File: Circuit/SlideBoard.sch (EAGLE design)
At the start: 24 parts

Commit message: Updated controller board to include BLE112 for easier soldering
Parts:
- R3: value 10k -> 50k
- U$1: value BLE113 -> BLE112; device Random:BLE113 -> temp:BLE112
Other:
- moved on the sheet: CAM, FOCUS, LIM, R3, R5, R6, RESET, SHUTTER, UART

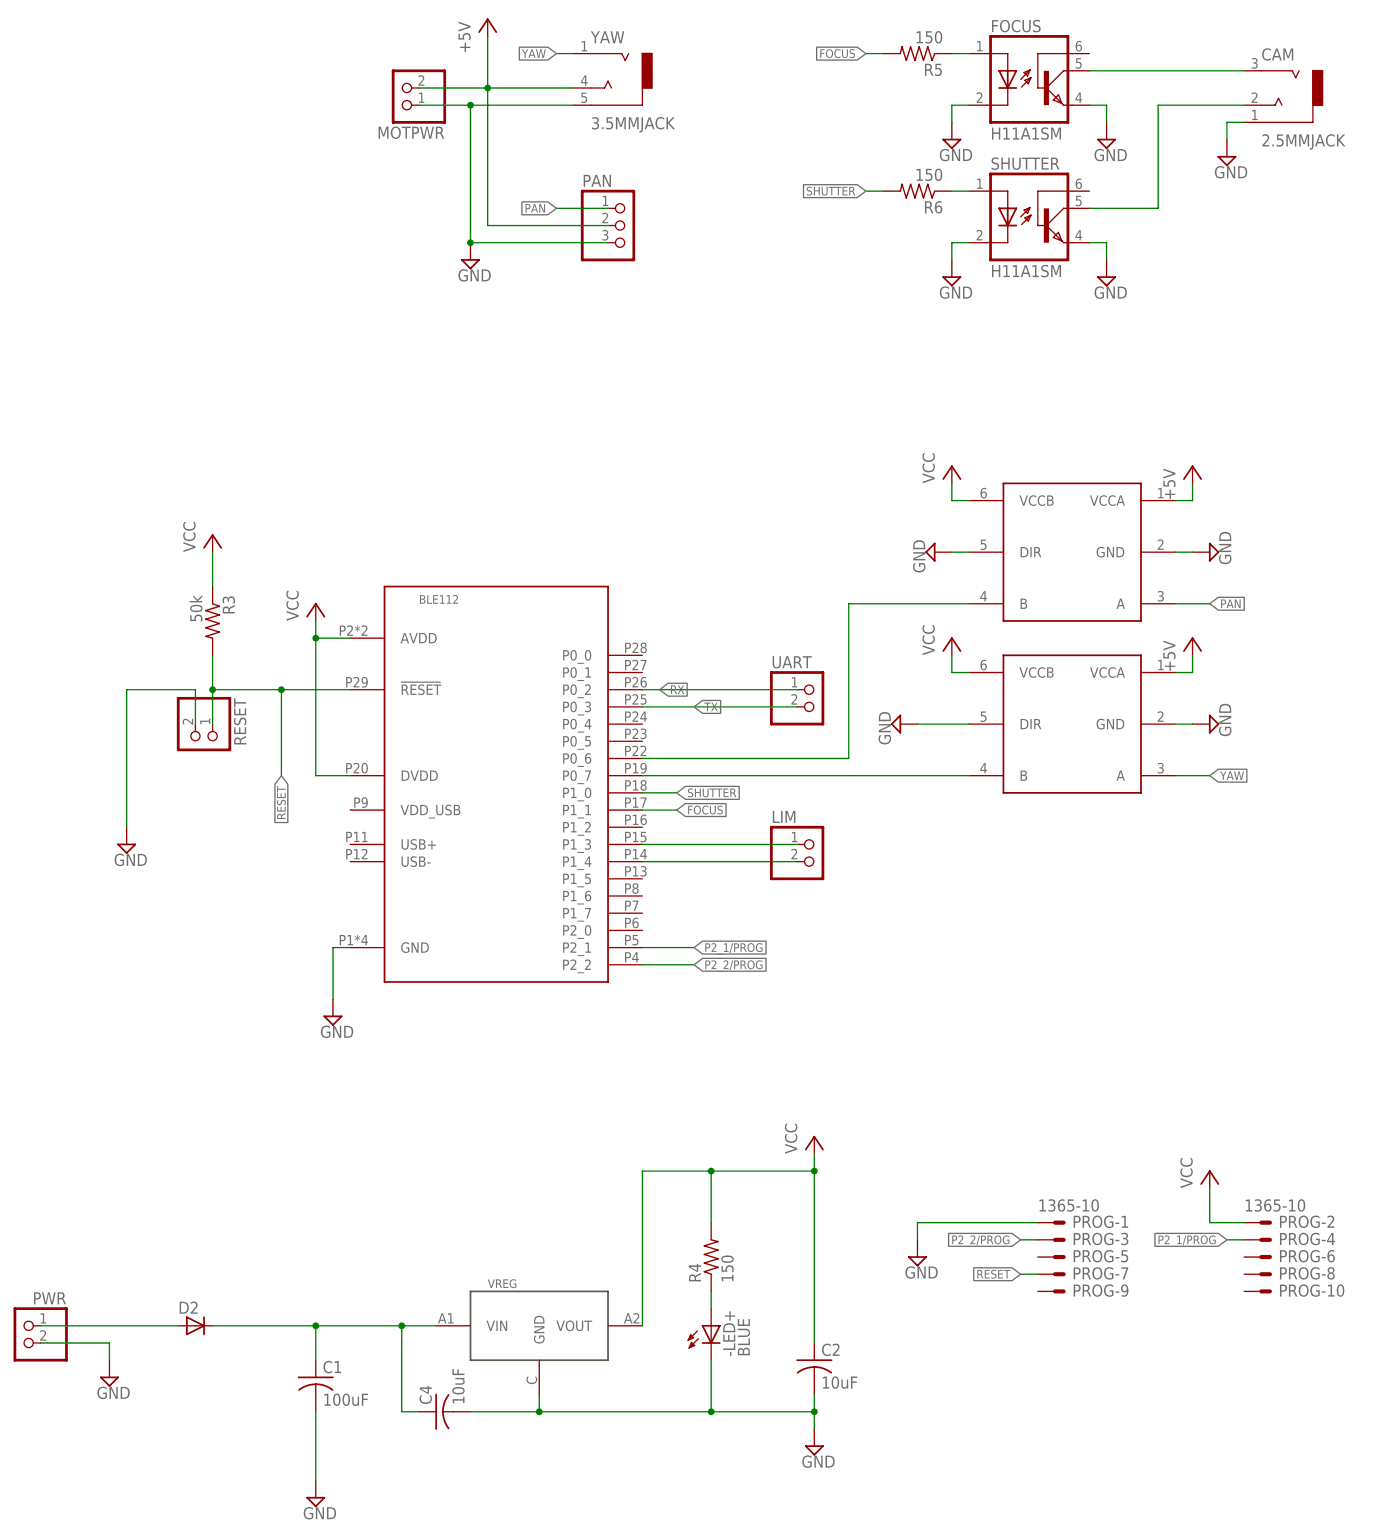
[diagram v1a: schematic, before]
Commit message: Updated circuit shematic to reflect current working board version
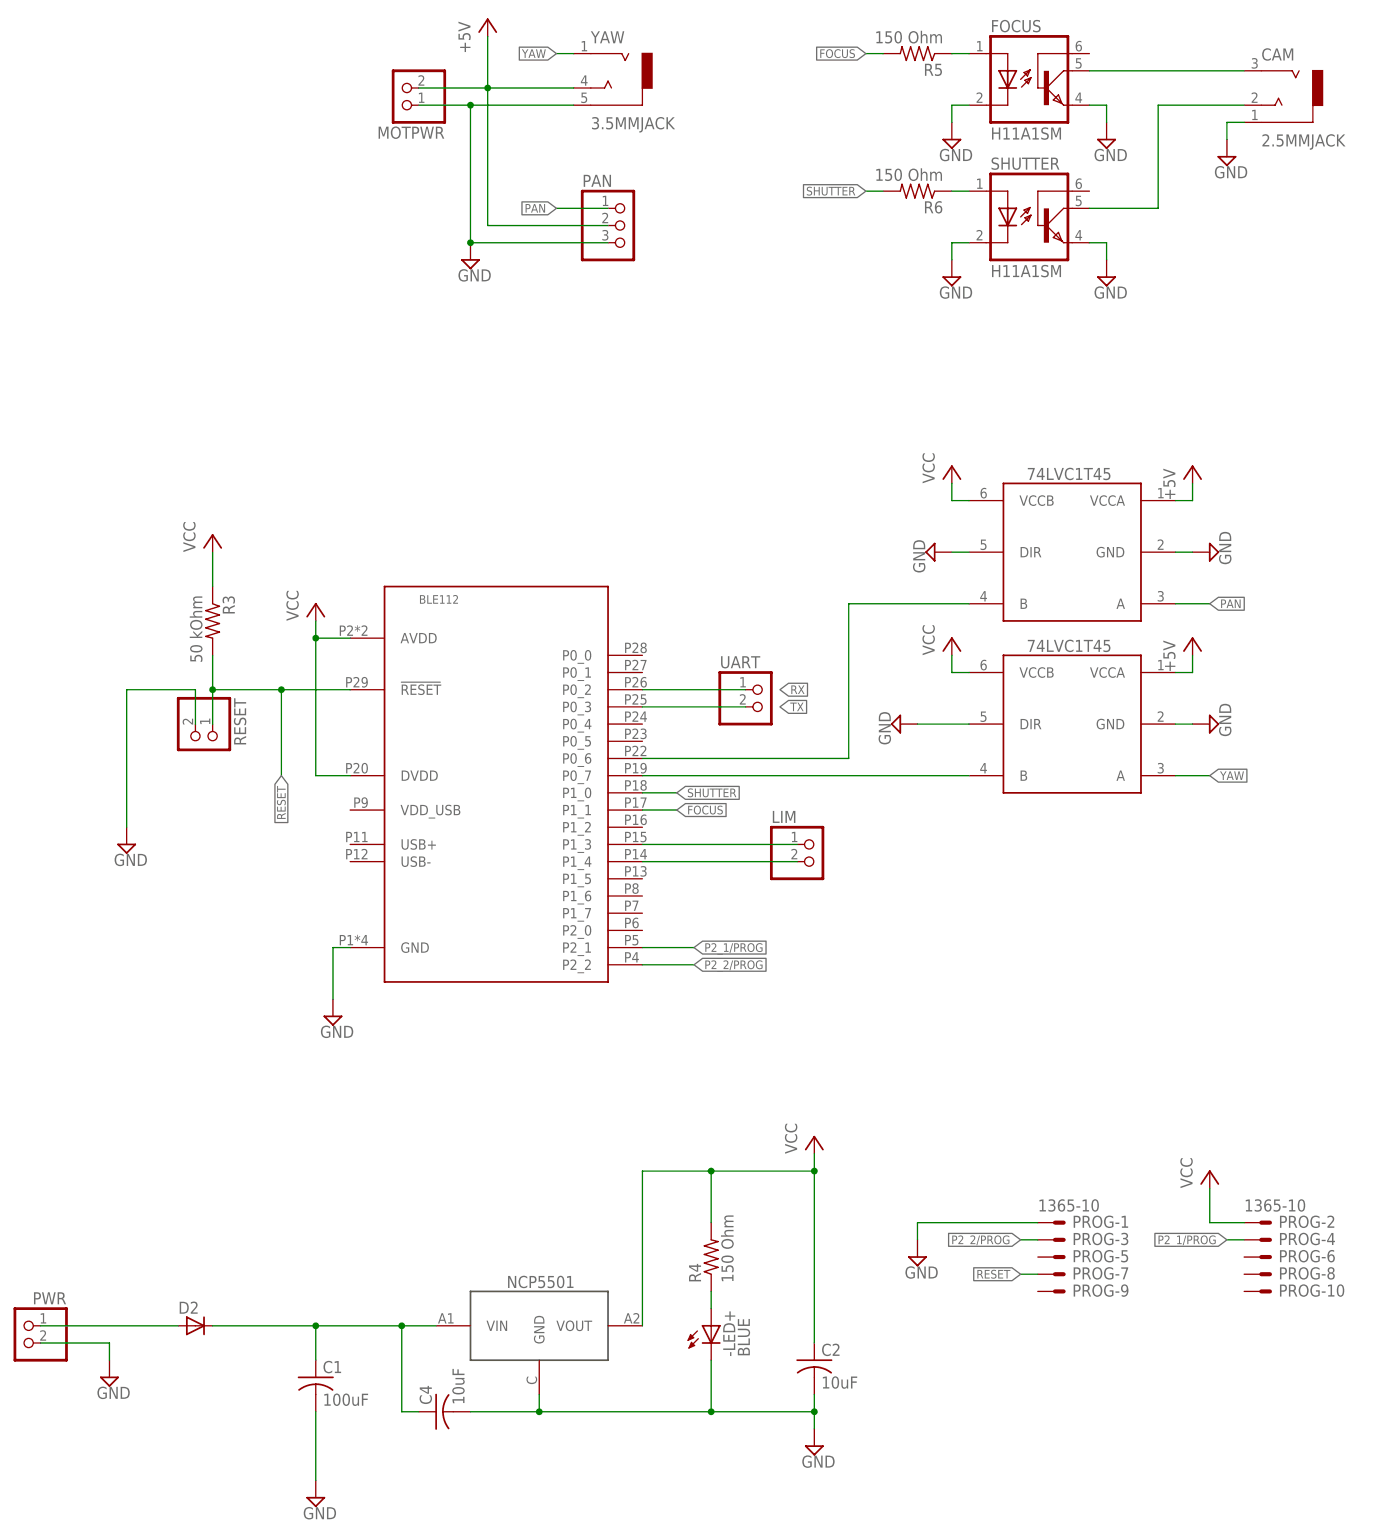
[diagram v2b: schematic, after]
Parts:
- R3: value 50k -> 50 kOhm
- R4, R5, R6: value 150 -> 150 Ohm
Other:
- moved on the sheet: UART
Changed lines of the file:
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@@
 <?xml version="1.0" encoding="utf-8"?>
 <!DOCTYPE eagle SYSTEM "eagle.dtd">
-<eagle version="7.6.0">
+<eagle version="7.5.0">
 <drawing>
 <settings>
@@
 <part name="SUPPLY9" library="supply2" deviceset="GND" device=""/>
 <part name="P+4" library="supply1" deviceset="VCC" device=""/>
-<part name="R3" library="rcl" deviceset="R-US_" device="R0603" value="50k"/>
+<part name="R3" library="rcl" deviceset="R-US_" device="R0603" value="50 kOhm"/>
 <part name="P+5" library="supply1" deviceset="VCC" device=""/>
 <part name="U$3" library="Random" deviceset="NCP5501" device=""/>
@@
 <part name="SUPPLY5" library="supply2" deviceset="GND" device=""/>
 <part name="SUPPLY14" library="supply2" deviceset="GND" device=""/>
-<part name="R4" library="resistor" deviceset="R-US_" device="R0402" value="150"/>
+<part name="R4" library="resistor" deviceset="R-US_" device="R0402" value="150 Ohm"/>
 <part name="-LED+" library="led" deviceset="LED" device="CHIP-LED0603" value="BLUE"/>
 <part name="PWR" library="pinhead" deviceset="PINHD-1X2" device=""/>
@@
 <part name="FOCUS" library="optocoupler" deviceset="H11A*?M" device="S" technology="1"/>
 <part name="SHUTTER" library="optocoupler" deviceset="H11A*?M" device="S" technology="1"/>
-<part name="R5" library="resistor" deviceset="R-US_" device="R0402" value="150"/>
-<part name="R6" library="resistor" deviceset="R-US_" device="R0402" value="150"/>
+<part name="R5" library="resistor" deviceset="R-US_" device="R0402" value="150 Ohm"/>
+<part name="R6" library="resistor" deviceset="R-US_" device="R0402" value="150 Ohm"/>
 <part name="SUPPLY1" library="supply2" deviceset="GND" device=""/>
 <part name="SUPPLY2" library="supply2" deviceset="GND" device=""/>
@@
 <instance part="P+10" gate="1" x="68.58" y="208.28"/>
 <instance part="LIM" gate="G$1" x="116.84" y="83.82"/>
-<instance part="UART" gate="G$1" x="116.84" y="106.68"/>
+<instance part="UART" gate="G$1" x="109.22" y="106.68"/>
 <instance part="CAM" gate="G$1" x="185.42" y="195.58"/>
 </instances>
@@
 <segment>
 <pinref part="U$1" gate="G$1" pin="P0_2"/>
-<label x="93.98" y="109.22" size="1.27" layer="95" xref="yes"/>
+<label x="111.76" y="109.22" size="1.27" layer="95" xref="yes"/>
 <pinref part="UART" gate="G$1" pin="1"/>
-<wire x1="91.44" y1="109.22" x2="114.3" y2="109.22" width="0.1524" layer="91"/>
+<wire x1="91.44" y1="109.22" x2="106.68" y2="109.22" width="0.1524" layer="91"/>
 </segment>
 </net>
@@
 <segment>
 <pinref part="U$1" gate="G$1" pin="P0_3"/>
-<label x="99.06" y="106.68" size="1.27" layer="95" xref="yes"/>
+<label x="111.76" y="106.68" size="1.27" layer="95" xref="yes"/>
 <pinref part="UART" gate="G$1" pin="2"/>
-<wire x1="114.3" y1="106.68" x2="91.44" y2="106.68" width="0.1524" layer="91"/>
-</segment>
-</net>
+<wire x1="106.68" y1="106.68" x2="91.44" y2="106.68" width="0.1524" layer="91"/>
+</segment>
+</net>
